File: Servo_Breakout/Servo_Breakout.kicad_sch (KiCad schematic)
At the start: 0 parts

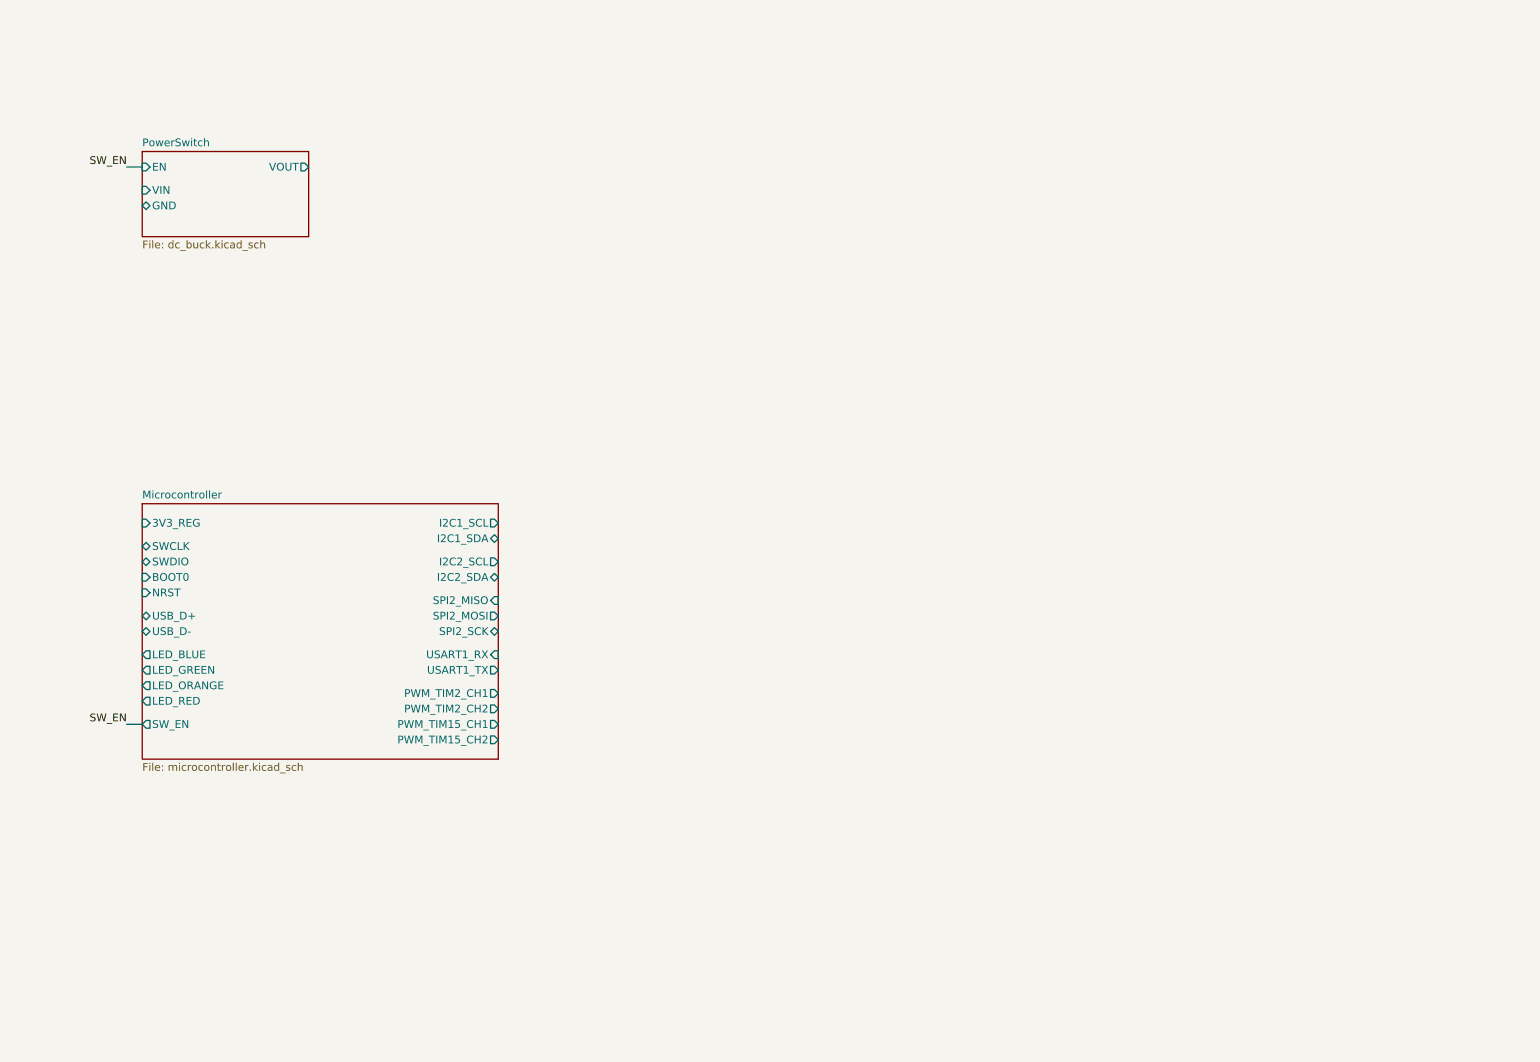
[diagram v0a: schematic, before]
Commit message: finalized schematic. footprints in progress
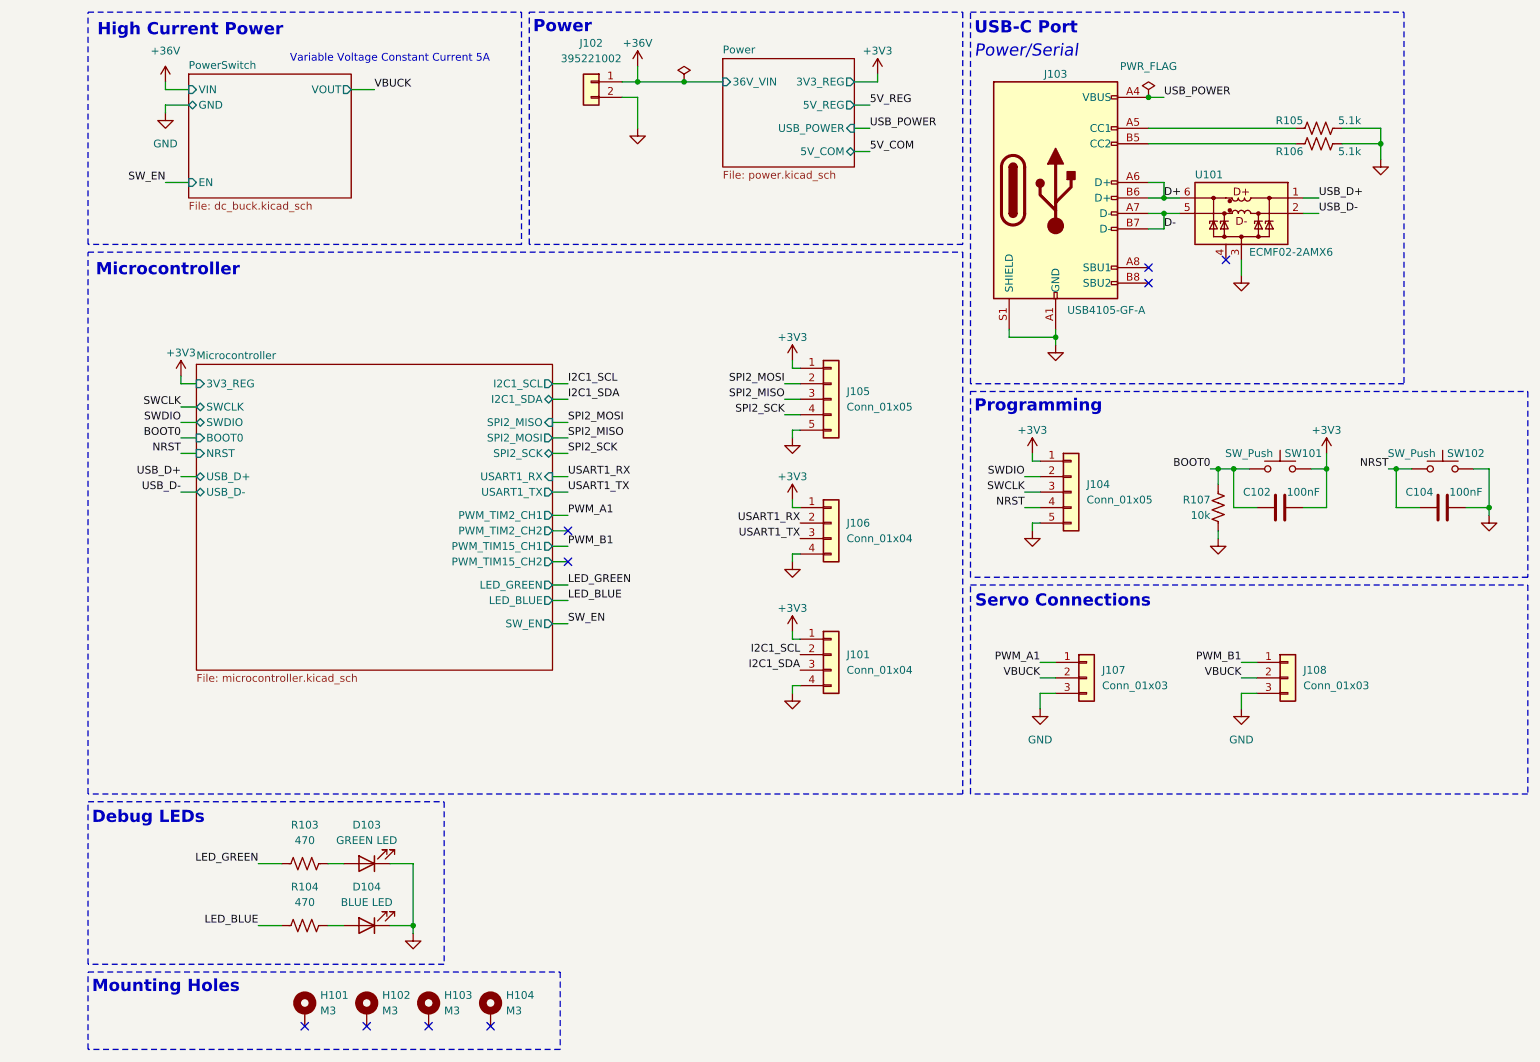
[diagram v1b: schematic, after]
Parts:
- added C102, C104: 100nF, Capacitor_SMD:C_0603_1608Metric, symbol Device:C
- added D103: GREEN LED, LED_SMD:LED_0603_1608Metric, symbol Device:LED
- added D104: BLUE LED, LED_SMD:LED_0603_1608Metric, symbol Device:LED
- added H101, H102, H103, H104: M3, MountingHole:MountingHole_3.2mm_M3_Pad_Via, symbol Mechanical:MountingHole_Pad
- added J101, J106: Conn_01x04, Connector_PinHeader_2.54mm:PinHeader_1x04_P2.54mm_Vertical, symbol Connector_Generic:Conn_01x04
- added J102: 395221002, Connector_Molex_TerminalBlock:Molex_39522-002_1x02_P5.00mm_Horizontal, symbol Connector_Generic:Conn_01x02
- added J103: USB4105-GF-A, Connector_USB:USB_C_Receptacle_GCT_USB4105-xx-A_16P_TopMnt_Horizontal, symbol Connector:USB_C_Receptacle_USB2.0_16P
- added J104, J105: Conn_01x05, Connector_PinHeader_2.54mm:PinHeader_1x05_P2.54mm_Vertical, symbol Connector_Generic:Conn_01x05
- added J107, J108: Conn_01x03, Connector_PinHeader_2.54mm:PinHeader_1x03_P2.54mm_Vertical, symbol Connector_Generic:Conn_01x03
- added R103, R104: 470, Resistor_SMD:R_0603_1608Metric, symbol Device:R_US
- added R105, R106: 5.1k, Resistor_SMD:R_0603_1608Metric, symbol Device:R_US
- added R107: 10k, Resistor_SMD:R_0603_1608Metric, symbol Device:R_US
- added SW101, SW102: SW_Push, Button_Switch_SMD:SW_SPST_FSMSM, symbol Switch:SW_Push
- added U101: ECMF02-2AMX6, Package_DFN_QFN:ST_UQFN-6L_1.5x1.7mm_P0.5mm, symbol Power_Protection:ECMF02-2AMX6
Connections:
- new net: D103.2 (A), R103.2
- new net: D104.2 (A), R104.2
- new net: J103.B5 (CC2), R106.1
- new net: J103.A5 (CC1), R105.1
- new net +36V: J102.1 (Pin_1)
- new net +3V3: C102.2, J101.1 (Pin_1), J104.1 (Pin_1), J105.1 (Pin_1), J106.1 (Pin_1), SW101.2
- new net BOOT0: C102.1, R107.1, SW101.1
- new net D+: J103.A6 (D+), J103.B6 (D+), U101.6 (D+_out)
- new net D-: J103.A7 (D-), J103.B7 (D-), U101.5 (D-_out)
- new net GND: C104.2, D103.1 (K), D104.1 (K), J101.4 (Pin_4), J102.2 (Pin_2), J103.A1 (GND), J103.A12 (GND), J103.B1 (GND), J103.B12 (GND), J103.S1 (SHIELD), J104.5 (Pin_5), J105.5 (Pin_5), J106.4 (Pin_4), J107.3 (Pin_3), J108.3 (Pin_3), R105.2, R106.2, R107.2, SW102.2, U101.3 (GND)
- new net I2C1_SCL: J101.2 (Pin_2)
- new net I2C1_SDA: J101.3 (Pin_3)
- new net LED_BLUE: R104.1
- new net LED_GREEN: R103.1
- new net NRST: C104.1, J104.4 (Pin_4), SW102.1
- new net PWM_A1: J107.1 (Pin_1)
- new net PWM_B1: J108.1 (Pin_1)
- new net SPI2_MISO: J105.3 (Pin_3)
- new net SPI2_MOSI: J105.2 (Pin_2)
- new net SPI2_SCK: J105.4 (Pin_4)
- new net SWCLK: J104.3 (Pin_3)
- new net SWDIO: J104.2 (Pin_2)
- new net USART1_RX: J106.2 (Pin_2)
- new net USART1_TX: J106.3 (Pin_3)
- new net USB_D+: U101.1 (D+_in)
- new net USB_D-: U101.2 (D-_in)
- new net USB_POWER: J103.A4 (VBUS), J103.A9 (VBUS), J103.B4 (VBUS), J103.B9 (VBUS)
- new net VBUCK: J107.2 (Pin_2), J108.2 (Pin_2)
- no-connect marks 0 -> 9
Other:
- added sheet Power (power.kicad_sch)
- sheet Microcontroller ports: added none; removed I2C2_SCL, I2C2_SDA, LED_ORANGE, LED_RED
- note added: "Debug LEDs"
- note added: "High Current Power"
- note added: "Microcontroller"
- note added: "Mounting Holes"
- note added: "Power"
- note added: "Power/Serial"
- note added: "Programming"
- note added: "Servo Connections"
- note added: "USB-C Port"
- note added: "Variable Voltage Constant Current 5A"

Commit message: replaced Micro with 555 Timer for PWM generation. completed most of layout
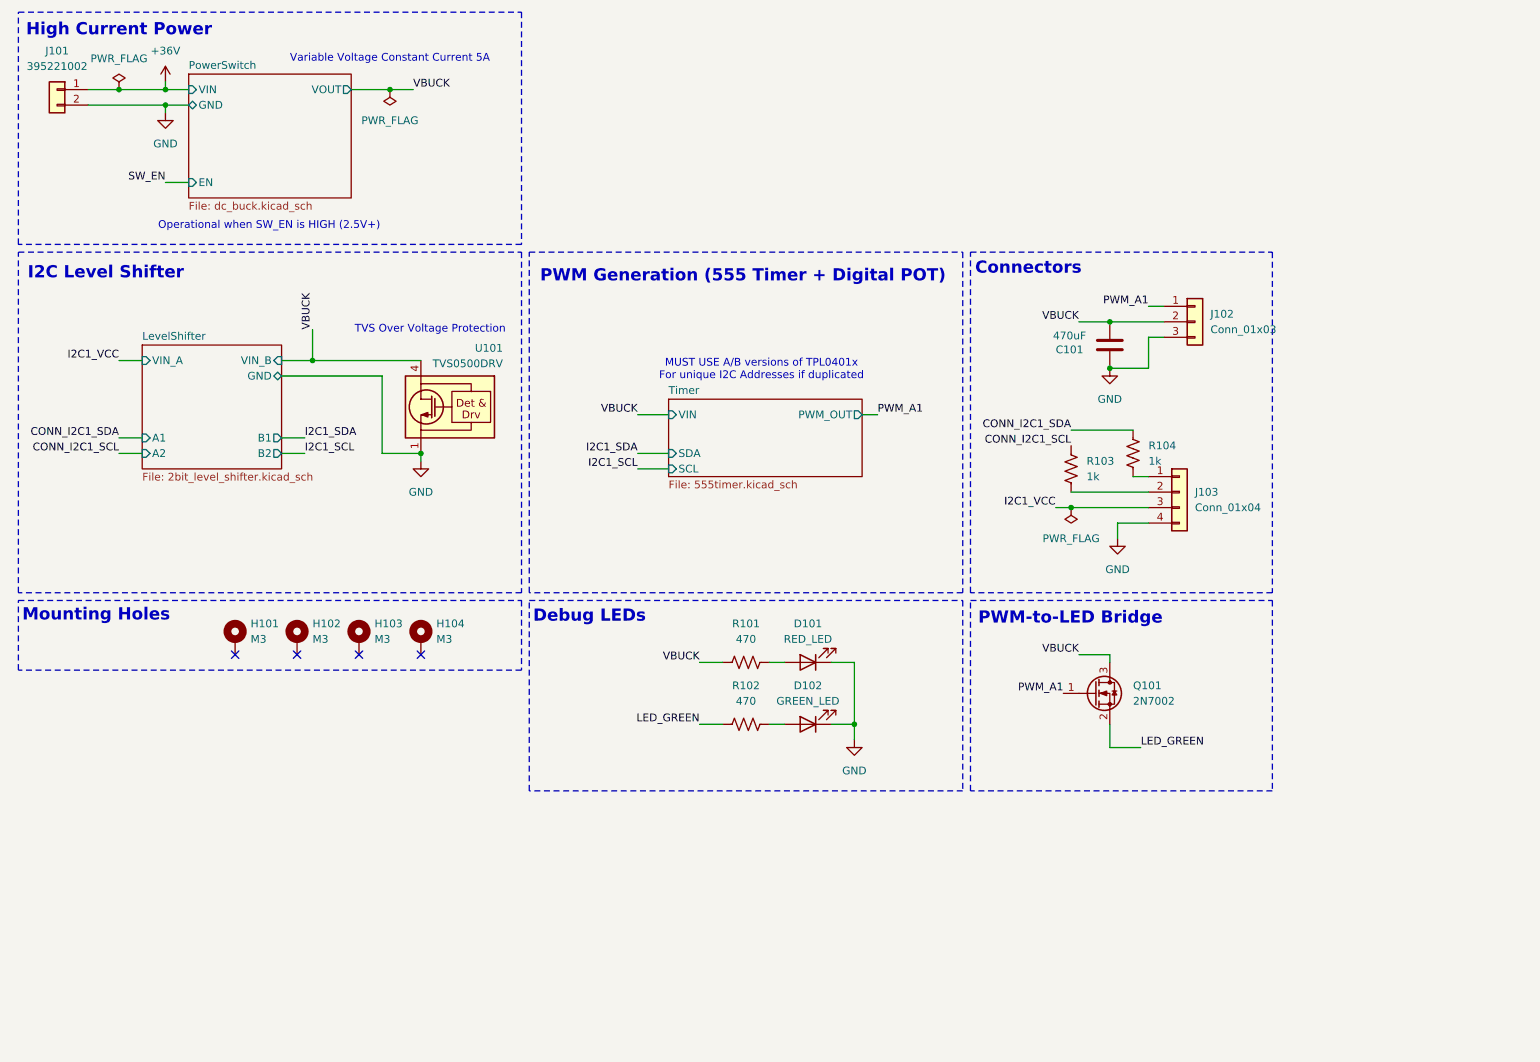
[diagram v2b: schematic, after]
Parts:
- removed C102, C104: 100nF, Capacitor_SMD:C_0603_1608Metric, symbol Device:C
- removed J101, J106: Conn_01x04, Connector_PinHeader_2.54mm:PinHeader_1x04_P2.54mm_Vertical, symbol Connector_Generic:Conn_01x04
- removed J103: USB4105-GF-A, Connector_USB:USB_C_Receptacle_GCT_USB4105-xx-A_16P_TopMnt_Horizontal, symbol Connector:USB_C_Receptacle_USB2.0_16P
- removed J104, J105: Conn_01x05, Connector_PinHeader_2.54mm:PinHeader_1x05_P2.54mm_Vertical, symbol Connector_Generic:Conn_01x05
- removed J108: Conn_01x03, Connector_PinHeader_2.54mm:PinHeader_1x03_P2.54mm_Vertical, symbol Connector_Generic:Conn_01x03
- removed R105, R106: 5.1k, Resistor_SMD:R_0603_1608Metric, symbol Device:R_US
- removed R107: 10k, Resistor_SMD:R_0603_1608Metric, symbol Device:R_US
- removed SW101, SW102: SW_Push, Button_Switch_SMD:SW_SPST_FSMSM, symbol Switch:SW_Push
- removed U101: ECMF02-2AMX6, Package_DFN_QFN:ST_UQFN-6L_1.5x1.7mm_P0.5mm, symbol Power_Protection:ECMF02-2AMX6
- added C101: 470uF, Capacitor_THT:C_Radial_D10.0mm_H20.0mm_P5.00mm, symbol Device:C
- added J103: Conn_01x04, Connector_PinHeader_2.54mm:PinHeader_1x04_P2.54mm_Vertical, symbol Connector_Generic:Conn_01x04
- added Q101: 2N7002, Package_TO_SOT_SMD:SOT-23, symbol Transistor_FET:2N7002
- added R103, R104: 1k, Resistor_SMD:R_0805_2012Metric_Pad1.20x1.40mm_HandSolder, symbol Device:R_US
- added U101: TVS0500DRV, Package_SON:WSON-6-1EP_2x2mm_P0.65mm_EP1x1.6mm, symbol Power_Protection:TVS0500DRV
- D101: renamed from D103; value GREEN LED -> RED_LED
- D102: renamed from D104; value BLUE LED -> GREEN_LED
- R101: renamed from R103; footprint Resistor_SMD:R_0603_1608Metric -> Resistor_SMD:R_0805_2012Metric_Pad1.20x1.40mm_HandSolder
- R102: renamed from R104; footprint Resistor_SMD:R_0603_1608Metric -> Resistor_SMD:R_0805_2012Metric_Pad1.20x1.40mm_HandSolder
- renumbered J102 to J101, J107 to J102
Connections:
- net LED_BLUE is gone; now on net LED_GREEN: R102.1
- net GND: now also C101.2, J103.4 (Pin_4), U101.1 (GND), U101.2 (GND), U101.3 (GND), U101.7 (GND)
- net LED_GREEN: now also Q101.2 (S); no longer R101.1
- net PWM_A1: now also Q101.1 (G)
- net VBUCK: now also R101.1, C101.1, Q101.3 (D), U101.4 (IN), U101.5 (IN), U101.6 (IN)
- new net: J103.1 (Pin_1), R104.2
- new net: J103.2 (Pin_2), R103.2
- new net CONN_I2C1_SCL: R103.1
- new net CONN_I2C1_SDA: R104.1
- new net I2C1_VCC: J103.3 (Pin_3)
- no-connect marks 9 -> 4
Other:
- removed sheet Microcontroller
- removed sheet Power
- added sheet LevelShifter (2bit_level_shifter.kicad_sch)
- added sheet Timer (555timer.kicad_sch)
- note added: "Connectors"
- note added: "I2C Level Shifter"
- note added: "MUST USE A/B versions of TPL0401x For unique I2C Addresses if duplicated"
- note added: "Operational when SW_EN is HIGH (2.5V+)"
- note added: "PWM Generation (555 Timer + Digital POT)"
- note added: "PWM-to-LED Bridge"
- note added: "TVS Over Voltage Protection"
- note removed: "Microcontroller"
- note removed: "Power"
- note removed: "Power/Serial"
- note removed: "Programming"
- note removed: "Servo Connections"
- note removed: "USB-C Port"
- moved on the sheet: D101, D102, H101, H102, H103, H104, J101, J102, R101, R102

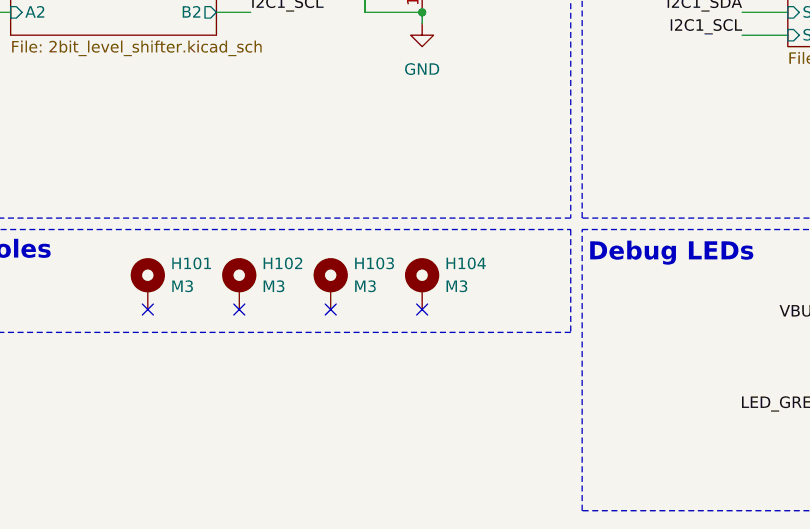
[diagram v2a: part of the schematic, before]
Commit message: Finalized layout and silkscreen
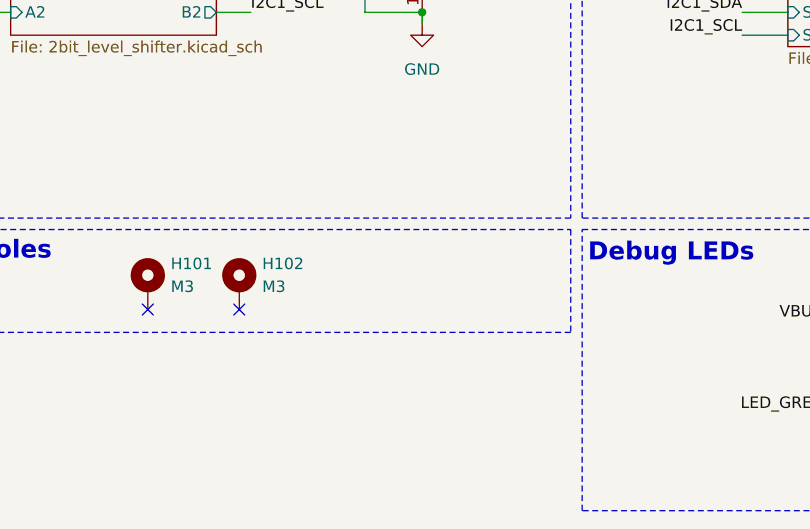
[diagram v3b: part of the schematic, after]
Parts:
- removed H103, H104: M3, MountingHole:MountingHole_3.2mm_M3_Pad_Via, symbol Mechanical:MountingHole_Pad
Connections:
- no-connect marks 4 -> 2
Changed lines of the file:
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@@
-	)
-	(no_connect
-		(at 101.6 119.38)
 	)
 	(no_connect
@@
 	)
 	(no_connect
-		(at 91.44 119.38)
-	)
-	(no_connect
 		(at 71.12 119.38)
 	)
@@
 			)
 			(justify right bottom)
-		)
-	)
-	(symbol
-		(lib_id "Mechanical:MountingHole_Pad")
-		(at 91.44 116.84 0)
-		(unit 1)
-		(exclude_from_sim no)
-		(in_bom yes)
-		(on_board yes)
-		(dnp no)
-		(property "Reference" "H103"
-			(at 93.98 114.3 0)
-			(effects
-				(font
-					(size 1.27 1.27)
-				)
-				(justify left)
-			)
-		)
-		(property "Value" "M3"
-			(at 93.98 116.84 0)
-			(effects
-				(font
-					(size 1.27 1.27)
-				)
-				(justify left)
-			)
-		)
-		(property "Footprint" "MountingHole:MountingHole_3.2mm_M3_Pad_Via"
-			(at 91.44 116.84 0)
-			(effects
-				(font
-					(size 1.27 1.27)
-				)
-				(hide yes)
-			)
-		)
-		(property "Datasheet" "~"
-			(at 91.44 116.84 0)
-			(effects
-				(font
-					(size 1.27 1.27)
-				)
-				(hide yes)
-			)
-		)
-		(property "Description" ""
-			(at 91.44 116.84 0)
-			(effects
-				(font
-					(size 1.27 1.27)
-				)
-				(hide yes)
-			)
-		)
-		(pin "1"
-		)
-		(instances
-			(project "Servo_Breakout"
-				(path "/d50da23a-d62e-4014-ae89-4f18c8c8c668"
-					(reference "H103")
-					(unit 1)
-				)
-			)
 		)
 	)
@@
 					(unit 1)
 				)
-			)
-		)
-	)
-	(symbol
-		(lib_id "Mechanical:MountingHole_Pad")
-		(at 101.6 116.84 0)
-		(unit 1)
-		(exclude_from_sim no)
-		(in_bom yes)
-		(on_board yes)
-		(dnp no)
-		(property "Reference" "H104"
-			(at 104.14 114.3 0)
-			(effects
-				(font
-					(size 1.27 1.27)
-				)
-				(justify left)
-			)
-		)
-		(property "Value" "M3"
-			(at 104.14 116.84 0)
-			(effects
-				(font
-					(size 1.27 1.27)
-				)
-				(justify left)
-			)
-		)
-		(property "Footprint" "MountingHole:MountingHole_3.2mm_M3_Pad_Via"
-			(at 101.6 116.84 0)
-			(effects
-				(font
-					(size 1.27 1.27)
-				)
-				(hide yes)
-			)
-		)
-		(property "Datasheet" "~"
-			(at 101.6 116.84 0)
-			(effects
-				(font
-					(size 1.27 1.27)
-				)
-				(hide yes)
-			)
-		)
-		(property "Description" ""
-			(at 101.6 116.84 0)
-			(effects
-				(font
-					(size 1.27 1.27)
-				)
-				(hide yes)
-			)
-		)
-		(pin "1"
-		)
-		(instances
-			(project "Servo_Breakout"
-				(path "/d50da23a-d62e-4014-ae89-4f18c8c8c668"
-					(reference "H104")
-					(unit 1)
-				)
